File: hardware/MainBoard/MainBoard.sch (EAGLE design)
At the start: 9 parts, among them IC1 A2F500M3G-FG256, IC3 CY62167EV30LL45BVX, J1 CON-71436-2164, J2 CON-71436-2164, J3 CON-FTSH-105-01-L-DV-K

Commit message: Library touch-up and basic placement on PCB.
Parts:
- removed IC3: CY62167EV30LL45BVX, MainBoard:CY62167EV30LL45BVX
- added J4: CON-ZX62R-B-5P, MainBoard:CON-ZX62R-B-5P
- added U2, U3: MAX19706-T4877-4, MainBoard:MAX19706-T4877-4
- added U4: USBLC6-2SC6, MainBoard:USBLC6-2SC6
- added U5: FT232HL, MainBoard:FT232HL
- added X1, X2: CON-SMA, MainBoard:CON-SMA
- renumbered IC1 to U1
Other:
- note added: "USB"
- note added: "USB connector"
- note removed: "SRAM MEMORY"

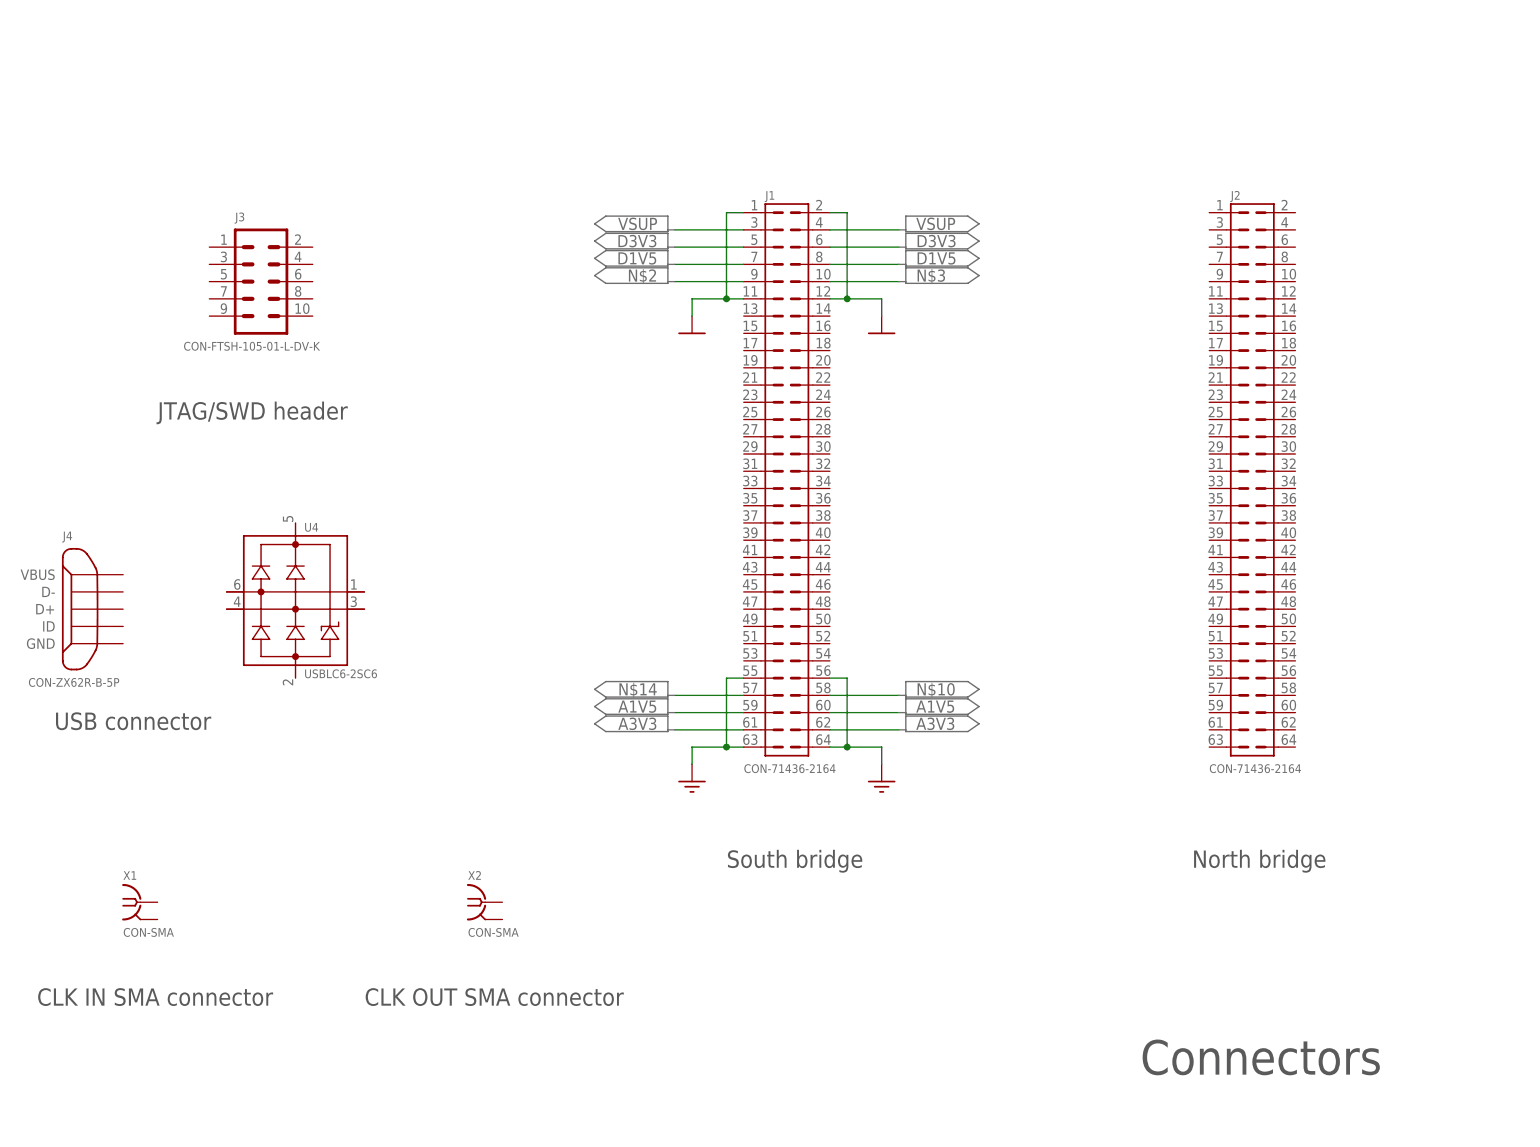
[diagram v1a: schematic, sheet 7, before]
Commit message: Updated the Mezzanine connectors in the Eagle library.
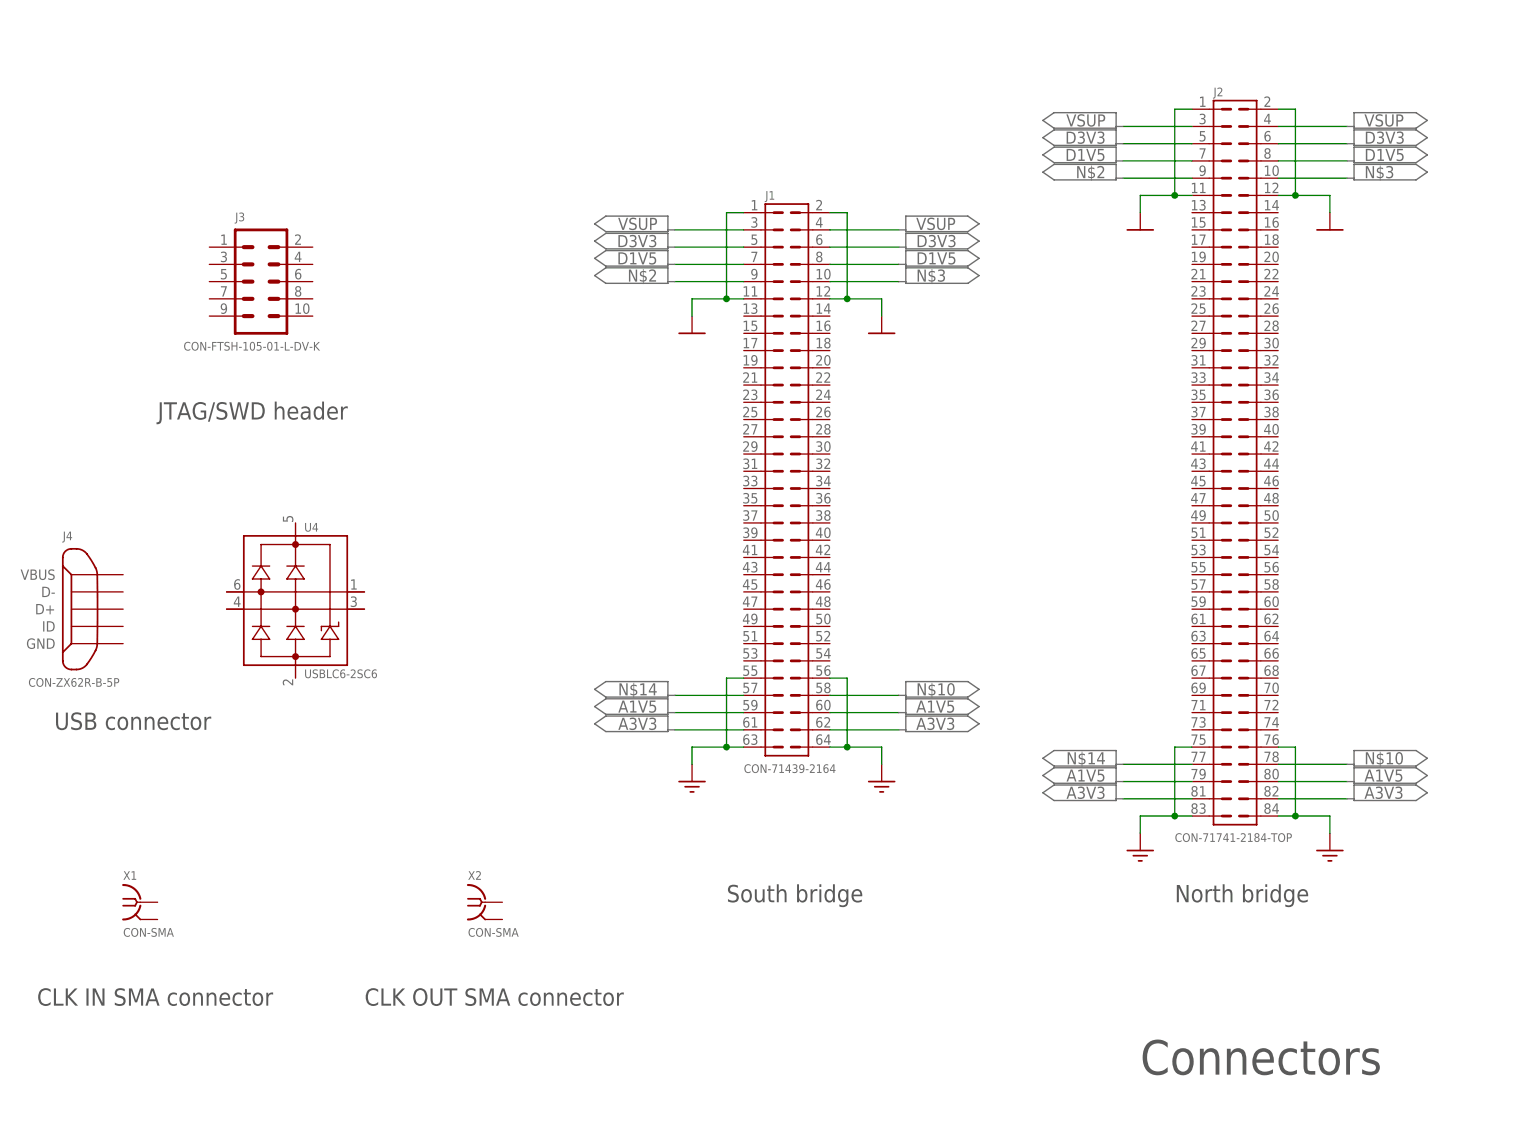
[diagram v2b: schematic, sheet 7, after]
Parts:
- J1: value CON-71436-2164 -> CON-71439-2164; device MainBoard:CON-71436-2164 -> MainBoard:CON-71439-2164; DIGI-KEY# (none) -> WM17222-ND; MPN (none) -> 71439-2164
- J2: value CON-71436-2164 -> CON-71741-2184-TOP; device MainBoard:CON-71436-2164 -> MainBoard:CON-71741-2184-TOP; DIGI-KEY# (none) -> WM3498CT-ND; MPN (none) -> 71741-0002
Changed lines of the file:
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@@
 <part name="FRAME4" library="powerboard" deviceset="FRAME-LETTER" device="" value=""/>
 <part name="FRAME6" library="powerboard" deviceset="FRAME-LETTER" device="" value=""/>
-<part name="J1" library="MainBoard" deviceset="CON-71436" device="64" technology="-21"/>
-<part name="J2" library="MainBoard" deviceset="CON-71436" device="64" technology="-21"/>
+<part name="J1" library="MainBoard" deviceset="CON-71439" device="64" technology="-21">
+<attribute name="DIGI-KEY#" value="WM17222-ND"/>
+<attribute name="MPN" value="71439-2164"/>
+</part>
+<part name="J2" library="MainBoard" deviceset="CON-71741" device="84-TOP" technology="-21">
+<attribute name="DIGI-KEY#" value="WM3498CT-ND"/>
+<attribute name="MPN" value="71741-0002"/>
+</part>
 <part name="J3" library="MainBoard" deviceset="CON-FTSH-105-01-L-DV-K" device=""/>
 <part name="U$5" library="MainBoard" deviceset="DGND" device=""/>
@@
 <part name="J4" library="MainBoard" deviceset="CON-ZX62R-B-5P" device=""/>
 <part name="U4" library="MainBoard" deviceset="USBLC6-2" device="SC6"/>
+<part name="U$13" library="MainBoard" deviceset="DGND" device=""/>
+<part name="PORT15" library="MainBoard" deviceset="PORT5" device=""/>
+<part name="PORT16" library="MainBoard" deviceset="PORT5" device=""/>
+<part name="PORT17" library="MainBoard" deviceset="PORT5" device=""/>
+<part name="PORT18" library="MainBoard" deviceset="PORT5" device=""/>
+<part name="U$14" library="MainBoard" deviceset="DGND" device=""/>
+<part name="PORT19" library="MainBoard" deviceset="PORT5" device=""/>
+<part name="PORT20" library="MainBoard" deviceset="PORT5" device=""/>
+<part name="PORT21" library="MainBoard" deviceset="PORT5" device=""/>
+<part name="PORT22" library="MainBoard" deviceset="PORT5" device=""/>
+<part name="U$15" library="MainBoard" deviceset="AGND" device=""/>
+<part name="PORT23" library="MainBoard" deviceset="PORT5" device=""/>
+<part name="PORT24" library="MainBoard" deviceset="PORT5" device=""/>
+<part name="PORT25" library="MainBoard" deviceset="PORT5" device=""/>
+<part name="U$16" library="MainBoard" deviceset="AGND" device=""/>
+<part name="PORT26" library="MainBoard" deviceset="PORT5" device=""/>
+<part name="PORT27" library="MainBoard" deviceset="PORT5" device=""/>
+<part name="PORT28" library="MainBoard" deviceset="PORT5" device=""/>
 </parts>
 <sheets>
@@
 <text x="187.96" y="20.32" size="5.08" layer="97">&gt;PAGE7</text>
 <text x="43.18" y="116.84" size="2.54" layer="97">JTAG/SWD header</text>
-<text x="127" y="50.8" size="2.54" layer="97">South bridge</text>
-<text x="195.58" y="50.8" size="2.54" layer="97">North bridge</text>
+<text x="127" y="45.72" size="2.54" layer="97">South bridge</text>
+<text x="193.04" y="45.72" size="2.54" layer="97">North bridge</text>
 <text x="25.4" y="30.48" size="2.54" layer="97">CLK IN SMA connector</text>
 <text x="73.66" y="30.48" size="2.54" layer="97">CLK OUT SMA connector</text>
@@
 <instance part="FRAME6" gate="G$2" x="147.32" y="0"/>
 <instance part="J1" gate="G$1" x="134.62" y="111.76"/>
-<instance part="J2" gate="G$1" x="203.2" y="111.76"/>
+<instance part="J2" gate="G$1" x="200.66" y="114.3"/>
 <instance part="J3" gate="G$1" x="58.42" y="137.16"/>
 <instance part="U$5" gate="G$1" x="121.92" y="129.54"/>
@@
 <instance part="J4" gate="G$1" x="35.56" y="88.9" rot="MR0"/>
 <instance part="U4" gate="G$1" x="63.5" y="91.44"/>
+<instance part="U$13" gate="G$1" x="187.96" y="144.78"/>
+<instance part="PORT15" gate="G$1" x="175.26" y="160.02" rot="MR0"/>
+<instance part="PORT16" gate="G$1" x="175.26" y="157.48" rot="MR0"/>
+<instance part="PORT17" gate="G$1" x="175.26" y="154.94" rot="MR0"/>
+<instance part="PORT18" gate="G$1" x="175.26" y="152.4" rot="MR0"/>
+<instance part="U$14" gate="G$1" x="215.9" y="144.78"/>
+<instance part="PORT19" gate="G$1" x="228.6" y="160.02"/>
+<instance part="PORT20" gate="G$1" x="228.6" y="157.48"/>
+<instance part="PORT21" gate="G$1" x="228.6" y="154.94"/>
+<instance part="PORT22" gate="G$1" x="228.6" y="152.4"/>
+<instance part="U$15" gate="G$1" x="187.96" y="53.34"/>
+<instance part="PORT23" gate="G$1" x="175.26" y="60.96" rot="MR0"/>
+<instance part="PORT24" gate="G$1" x="175.26" y="63.5" rot="MR0"/>
+<instance part="PORT25" gate="G$1" x="175.26" y="66.04" rot="MR0"/>
+<instance part="U$16" gate="G$1" x="215.9" y="53.34"/>
+<instance part="PORT26" gate="G$1" x="228.6" y="66.04"/>
+<instance part="PORT27" gate="G$1" x="228.6" y="63.5"/>
+<instance part="PORT28" gate="G$1" x="228.6" y="60.96"/>
 </instances>
 <busses>
@@
 <pinref part="J1" gate="G$1" pin="4"/>
 </segment>
+<segment>
+<wire x1="195.58" y1="160.02" x2="185.42" y2="160.02" width="0.1524" layer="91"/>
+<label x="182.88" y="160.02" size="1.778" layer="95" rot="MR0"/>
+</segment>
+<segment>
+<wire x1="208.28" y1="160.02" x2="218.44" y2="160.02" width="0.1524" layer="91"/>
+<label x="220.98" y="160.02" size="1.778" layer="95"/>
+</segment>
 </net>
 <net name="D3V3" class="0">
@@
 <pinref part="J1" gate="G$1" pin="6"/>
 </segment>
+<segment>
+<wire x1="195.58" y1="157.48" x2="185.42" y2="157.48" width="0.1524" layer="91"/>
+<label x="182.88" y="157.48" size="1.778" layer="95" rot="MR0"/>
+</segment>
+<segment>
+<wire x1="208.28" y1="157.48" x2="218.44" y2="157.48" width="0.1524" layer="91"/>
+<label x="220.98" y="157.48" size="1.778" layer="95"/>
+</segment>
 </net>
 <net name="D1V5" class="0">
@@
 <label x="154.94" y="139.7" size="1.778" layer="95"/>
 <pinref part="J1" gate="G$1" pin="8"/>
+</segment>
+<segment>
+<wire x1="195.58" y1="154.94" x2="185.42" y2="154.94" width="0.1524" layer="91"/>
+<label x="182.88" y="154.94" size="1.778" layer="95" rot="MR0"/>
+</segment>
+<segment>
+<wire x1="208.28" y1="154.94" x2="218.44" y2="154.94" width="0.1524" layer="91"/>
+<label x="220.98" y="154.94" size="1.778" layer="95"/>
 </segment>
 </net>
@@
 <pinref part="J1" gate="G$1" pin="2"/>
 </segment>
+<segment>
+<wire x1="195.58" y1="149.86" x2="193.04" y2="149.86" width="0.1524" layer="91"/>
+<wire x1="195.58" y1="162.56" x2="193.04" y2="162.56" width="0.1524" layer="91"/>
+<wire x1="193.04" y1="149.86" x2="193.04" y2="162.56" width="0.1524" layer="91"/>
+<wire x1="193.04" y1="149.86" x2="187.96" y2="149.86" width="0.1524" layer="91"/>
+<wire x1="187.96" y1="149.86" x2="187.96" y2="147.32" width="0.1524" layer="91"/>
+<junction x="193.04" y="149.86"/>
+<pinref part="U$13" gate="G$1" pin="DGND"/>
+</segment>
+<segment>
+<wire x1="208.28" y1="149.86" x2="210.82" y2="149.86" width="0.1524" layer="91"/>
+<wire x1="210.82" y1="149.86" x2="215.9" y2="149.86" width="0.1524" layer="91"/>
+<wire x1="215.9" y1="149.86" x2="215.9" y2="147.32" width="0.1524" layer="91"/>
+<wire x1="208.28" y1="162.56" x2="210.82" y2="162.56" width="0.1524" layer="91"/>
+<wire x1="210.82" y1="162.56" x2="210.82" y2="149.86" width="0.1524" layer="91"/>
+<junction x="210.82" y="149.86"/>
+<pinref part="U$14" gate="G$1" pin="DGND"/>
+</segment>
 </net>
 <net name="N$2" class="0">
@@
 <pinref part="J1" gate="G$1" pin="9"/>
 </segment>
+<segment>
+<wire x1="185.42" y1="152.4" x2="195.58" y2="152.4" width="0.1524" layer="91"/>
+<label x="182.88" y="152.4" size="1.778" layer="95" rot="MR0"/>
+</segment>
 </net>
 <net name="N$3" class="0">
@@
 <pinref part="J1" gate="G$1" pin="10"/>
 </segment>
+<segment>
+<wire x1="218.44" y1="152.4" x2="208.28" y2="152.4" width="0.1524" layer="91"/>
+<label x="220.98" y="152.4" size="1.778" layer="95"/>
+</segment>
 </net>
 <net name="A1V5" class="0">
@@
 <pinref part="J1" gate="G$1" pin="59"/>
 </segment>
+<segment>
+<wire x1="195.58" y1="63.5" x2="185.42" y2="63.5" width="0.1524" layer="91"/>
+<label x="182.88" y="63.5" size="1.778" layer="95" rot="MR0"/>
+</segment>
+<segment>
+<wire x1="208.28" y1="63.5" x2="218.44" y2="63.5" width="0.1524" layer="91"/>
+<label x="220.98" y="63.5" size="1.778" layer="95"/>
+</segment>
 </net>
 <net name="N$10" class="0">
@@
 <pinref part="J1" gate="G$1" pin="58"/>
 </segment>
+<segment>
+<wire x1="208.28" y1="66.04" x2="218.44" y2="66.04" width="0.1524" layer="91"/>
+<label x="220.98" y="66.04" size="1.778" layer="95"/>
+</segment>
 </net>
 <net name="A3V3" class="0">
@@
 <pinref part="J1" gate="G$1" pin="62"/>
 </segment>
+<segment>
+<wire x1="195.58" y1="60.96" x2="185.42" y2="60.96" width="0.1524" layer="91"/>
+<label x="182.88" y="60.96" size="1.778" layer="95" rot="MR0"/>
+</segment>
+<segment>
+<wire x1="208.28" y1="60.96" x2="218.44" y2="60.96" width="0.1524" layer="91"/>
+<label x="220.98" y="60.96" size="1.778" layer="95"/>
+</segment>
 </net>
 <net name="N$14" class="0">
@@
 <label x="116.84" y="76.2" size="1.778" layer="95" rot="MR0"/>
 <pinref part="J1" gate="G$1" pin="57"/>
+</segment>
+<segment>
+<wire x1="195.58" y1="66.04" x2="185.42" y2="66.04" width="0.1524" layer="91"/>
+<label x="182.88" y="66.04" size="1.778" layer="95" rot="MR0"/>
 </segment>
 </net>
@@
 <pinref part="J1" gate="G$1" pin="56"/>
 </segment>
-</net>
+<segment>
+<wire x1="195.58" y1="58.42" x2="193.04" y2="58.42" width="0.1524" layer="91"/>
+<wire x1="193.04" y1="58.42" x2="187.96" y2="58.42" width="0.1524" layer="91"/>
+<wire x1="187.96" y1="58.42" x2="187.96" y2="55.88" width="0.1524" layer="91"/>
+<wire x1="195.58" y1="68.58" x2="193.04" y2="68.58" width="0.1524" layer="91"/>
+<wire x1="193.04" y1="68.58" x2="193.04" y2="58.42" width="0.1524" layer="91"/>
+<junction x="193.04" y="58.42"/>
+<pinref part="U$15" gate="G$1" pin="AGND"/>
+</segment>
+<segment>
+<wire x1="208.28" y1="58.42" x2="210.82" y2="58.42" width="0.1524" layer="91"/>
+<wire x1="210.82" y1="58.42" x2="215.9" y2="58.42" width="0.1524" layer="91"/>
+<wire x1="215.9" y1="58.42" x2="215.9" y2="55.88" width="0.1524" layer="91"/>
+<wire x1="208.28" y1="68.58" x2="210.82" y2="68.58" width="0.1524" layer="91"/>
+<wire x1="210.82" y1="68.58" x2="210.82" y2="58.42" width="0.1524" layer="91"/>
+<junction x="210.82" y="58.42"/>
+<pinref part="U$16" gate="G$1" pin="AGND"/>
+</segment>
+</net>
